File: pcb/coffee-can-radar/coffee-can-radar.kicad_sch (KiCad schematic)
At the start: 0 parts

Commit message: Add vco, attenuator and pa
First time taking kicad for a spin, it is great! Feels very familiar for
someone coming from Altium.
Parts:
- added AT?: PAT1220-C-1DB-T5, ccr-footprints:ATTN_PAT1220-C-1DB-T5, symbol ccr-library:PAT1220-C-1DB-T5
- added U?: SST11LP12, ccr-footprints:QFN-16_EP_3x3_Pitch0.5mm, symbol ccr-library:SST11LP12
- added U?: HMC431LP4E, ccr-footprints:QFN50P400X400X100-25N, symbol ccr-library:HMC431LP4E
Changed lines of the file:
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@@
 (kicad_sch (version 20211123) (generator eeschema)
   (paper "A4")
+  (symbol (lib_id "ccr-library:SST11LP12") (at 130.81 43.18 0) (unit 1)
+    (in_bom yes) (on_board yes) (fields_autoplaced)
+    (property "Reference" "U?" (id 0) (at 138.43 38.1 0))
+    (property "Value" "SST11LP12" (id 1) (at 138.43 40.64 0))
+    (property "Footprint" "ccr-footprints:QFN-16_EP_3x3_Pitch0.5mm" (id 2) (at 138.43 77.47 0)
+      (effects (font (size 1.27 1.27)) hide)
+    )
+    (property "Datasheet" "" (id 3) (at 130.81 43.18 0)
+      (effects (font (size 1.27 1.27)) hide)
+    )
+    (pin "1")
+    (pin "10")
+    (pin "11")
+    (pin "12")
+    (pin "13")
+    (pin "14")
+    (pin "15")
+    (pin "16")
+    (pin "16")
+    (pin "2")
+    (pin "3")
+    (pin "4")
+    (pin "5")
+    (pin "6")
+    (pin "7")
+    (pin "8")
+    (pin "9")
+  )
+  (symbol (lib_id "ccr-library:HMC431LP4E") (at 60.96 52.07 0) (unit 1)
+    (in_bom yes) (on_board yes) (fields_autoplaced)
+    (property "Reference" "U?" (id 0) (at 60.96 38.1 0))
+    (property "Value" "HMC431LP4E" (id 1) (at 60.96 40.64 0))
+    (property "Footprint" "ccr-footprints:QFN50P400X400X100-25N" (id 2) (at 50.8 66.04 0)
+      (effects (font (size 1.27 1.27)) (justify left bottom) hide)
+    )
+    (property "Datasheet" "" (id 3) (at 60.96 52.07 0)
+      (effects (font (size 1.27 1.27)) (justify left bottom) hide)
+    )
+    (property "MANUFACTURER" "Analog Devices" (id 4) (at 50.8 68.58 0)
+      (effects (font (size 1.27 1.27)) (justify left bottom) hide)
+    )
+    (pin "15")
+    (pin "16")
+    (pin "20")
+    (pin "22")
+    (pin "25")
+  )
+  (symbol (lib_id "ccr-library:PAT1220-C-1DB-T5") (at 106.68 50.8 0) (unit 1)
+    (in_bom yes) (on_board yes) (fields_autoplaced)
+    (property "Reference" "AT?" (id 0) (at 106.68 39.37 0))
+    (property "Value" "PAT1220-C-1DB-T5" (id 1) (at 106.68 41.91 0))
+    (property "Footprint" "ccr-footprints:ATTN_PAT1220-C-1DB-T5" (id 2) (at 109.22 60.96 0)
+      (effects (font (size 1.27 1.27)) (justify left bottom) hide)
+    )
+    (property "Datasheet" "" (id 3) (at 106.68 50.8 0)
+      (effects (font (size 1.27 1.27)) (justify left bottom) hide)
+    )
+    (property "MANUFACTURER" "SUSUMU" (id 4) (at 109.22 66.04 0)
+      (effects (font (size 1.27 1.27)) (justify left bottom) hide)
+    )
+    (property "STANDARD" "Manufacturer Recommendation" (id 5) (at 109.22 63.5 0)
+      (effects (font (size 1.27 1.27)) (justify left bottom) hide)
+    )
+    (pin "1")
+    (pin "2")
+    (pin "3")
+  )
   (sheet_instances
     (path "/" (page "1"))
   )
+  (symbol_instances
+    (path "/ecd19b5c-e315-4c28-8027-9f4a1f763db3"
+      (reference "AT?") (unit 1) (value "PAT1220-C-1DB-T5") (footprint "ccr-footprints:ATTN_PAT1220-C-1DB-T5")
+    )
+    (path "/52482f1c-9ada-4ff6-8246-b79e406c8266"
+      (reference "U?") (unit 1) (value "SST11LP12") (footprint "ccr-footprints:QFN-16_EP_3x3_Pitch0.5mm")
+    )
+    (path "/5be57fd5-b493-4486-8a3b-793a67150f96"
+      (reference "U?") (unit 1) (value "HMC431LP4E") (footprint "ccr-footprints:QFN50P400X400X100-25N")
+    )
+  )
 )

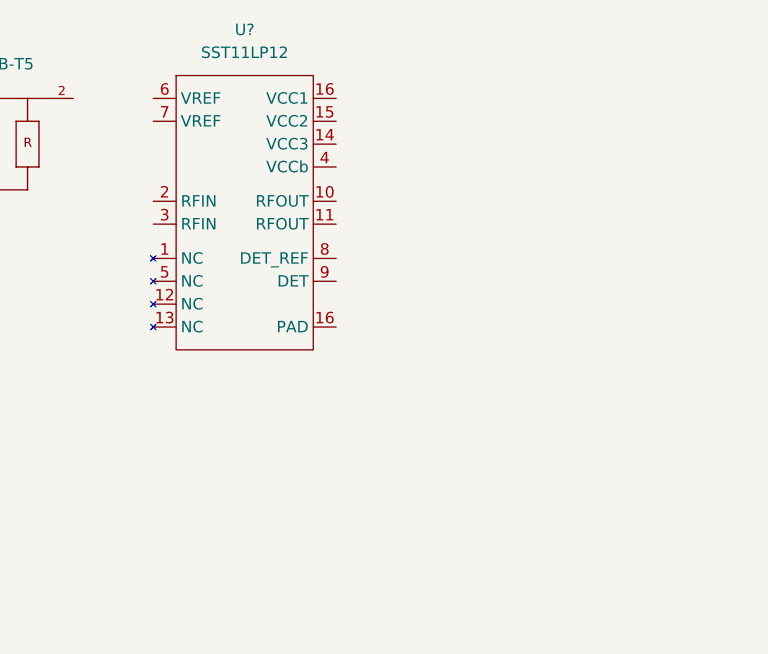
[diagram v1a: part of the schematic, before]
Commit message: Add mixer and pa
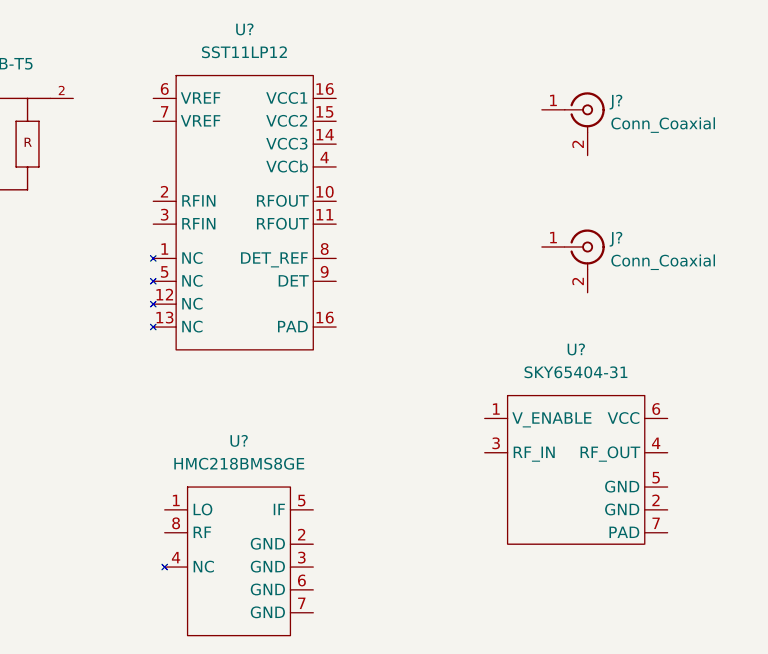
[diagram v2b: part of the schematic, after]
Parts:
- added J? (x2): Conn_Coaxial, symbol Connector:Conn_Coaxial
- added U?: SKY65404-31, ccr-footprints:SKY65404-31, symbol ccr-library:SKY65404-31
- added U?: HMC218BMS8GE, Package_SO:MSOP-8-1EP_3x3mm_P0.65mm_EP1.68x1.88mm, symbol ccr-library:HMC218BMS8GE
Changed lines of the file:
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@@
 (kicad_sch (version 20211123) (generator eeschema)
   (paper "A4")
+  (symbol (lib_id "Connector:Conn_Coaxial") (at 176.53 46.99 0) (unit 1)
+    (in_bom yes) (on_board yes) (fields_autoplaced)
+    (property "Reference" "J?" (id 0) (at 179.07 46.0131 0)
+      (effects (font (size 1.27 1.27)) (justify left))
+    )
+    (property "Value" "Conn_Coaxial" (id 1) (at 179.07 48.5531 0)
+      (effects (font (size 1.27 1.27)) (justify left))
+    )
+    (property "Footprint" "" (id 2) (at 176.53 46.99 0)
+      (effects (font (size 1.27 1.27)) hide)
+    )
+    (property "Datasheet" " ~" (id 3) (at 176.53 46.99 0)
+      (effects (font (size 1.27 1.27)) hide)
+    )
+    (pin "1")
+    (pin "2")
+  )
+  (symbol (lib_id "ccr-library:SKY65404-31") (at 167.64 78.74 0) (unit 1)
+    (in_bom yes) (on_board yes) (fields_autoplaced)
+    (property "Reference" "U?" (id 0) (at 175.26 73.66 0))
+    (property "Value" "SKY65404-31" (id 1) (at 175.26 76.2 0))
+    (property "Footprint" "ccr-footprints:SKY65404-31" (id 2) (at 181.61 99.06 0)
+      (effects (font (size 1.27 1.27)) hide)
+    )
+    (property "Datasheet" "" (id 3) (at 167.64 78.74 0)
+      (effects (font (size 1.27 1.27)) hide)
+    )
+    (pin "1")
+    (pin "2")
+    (pin "3")
+    (pin "4")
+    (pin "5")
+    (pin "6")
+    (pin "7")
+  )
   (symbol (lib_id "ccr-library:SST11LP12") (at 130.81 43.18 0) (unit 1)
     (in_bom yes) (on_board yes) (fields_autoplaced)
@@
     (pin "25")
   )
+  (symbol (lib_id "ccr-library:HMC218BMS8GE") (at 132.08 88.9 0) (unit 1)
+    (in_bom yes) (on_board yes) (fields_autoplaced)
+    (property "Reference" "U?" (id 0) (at 137.795 83.82 0))
+    (property "Value" "HMC218BMS8GE" (id 1) (at 137.795 86.36 0))
+    (property "Footprint" "Package_SO:MSOP-8-1EP_3x3mm_P0.65mm_EP1.68x1.88mm" (id 2) (at 139.7 109.22 0)
+      (effects (font (size 1.27 1.27)) hide)
+    )
+    (property "Datasheet" "" (id 3) (at 132.08 88.9 0)
+      (effects (font (size 1.27 1.27)) hide)
+    )
+    (pin "1")
+    (pin "2")
+    (pin "3")
+    (pin "4")
+    (pin "5")
+    (pin "6")
+    (pin "7")
+    (pin "8")
+  )
+  (symbol (lib_id "Connector:Conn_Coaxial") (at 176.53 62.23 0) (unit 1)
+    (in_bom yes) (on_board yes) (fields_autoplaced)
+    (property "Reference" "J?" (id 0) (at 179.07 61.2531 0)
+      (effects (font (size 1.27 1.27)) (justify left))
+    )
+    (property "Value" "Conn_Coaxial" (id 1) (at 179.07 63.7931 0)
+      (effects (font (size 1.27 1.27)) (justify left))
+    )
+    (property "Footprint" "" (id 2) (at 176.53 62.23 0)
+      (effects (font (size 1.27 1.27)) hide)
+    )
+    (property "Datasheet" " ~" (id 3) (at 176.53 62.23 0)
+      (effects (font (size 1.27 1.27)) hide)
+    )
+    (pin "1")
+    (pin "2")
+  )
   (symbol (lib_id "ccr-library:PAT1220-C-1DB-T5") (at 106.68 50.8 0) (unit 1)
     (in_bom yes) (on_board yes) (fields_autoplaced)
@@
       (reference "AT?") (unit 1) (value "PAT1220-C-1DB-T5") (footprint "ccr-footprints:ATTN_PAT1220-C-1DB-T5")
     )
+    (path "/36d17e07-64a7-424e-bc11-f3b0290e93d6"
+      (reference "J?") (unit 1) (value "Conn_Coaxial") (footprint "")
+    )
+    (path "/ea4f39a8-620c-4c83-99a6-875278db5cdb"
+      (reference "J?") (unit 1) (value "Conn_Coaxial") (footprint "")
+    )
+    (path "/40638cd4-269b-4c75-a7a3-ad362dca6ed3"
+      (reference "U?") (unit 1) (value "SKY65404-31") (footprint "ccr-footprints:SKY65404-31")
+    )
     (path "/52482f1c-9ada-4ff6-8246-b79e406c8266"
       (reference "U?") (unit 1) (value "SST11LP12") (footprint "ccr-footprints:QFN-16_EP_3x3_Pitch0.5mm")
@@
       (reference "U?") (unit 1) (value "HMC431LP4E") (footprint "ccr-footprints:QFN50P400X400X100-25N")
     )
+    (path "/77b6919d-9a80-4972-8981-2d6bb82e8279"
+      (reference "U?") (unit 1) (value "HMC218BMS8GE") (footprint "Package_SO:MSOP-8-1EP_3x3mm_P0.65mm_EP1.68x1.88mm")
+    )
   )

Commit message: Update atten
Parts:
- removed AT?: PAT1220-C-1DB-T5, ccr-footprints:ATTN_PAT1220-C-1DB-T5, symbol ccr-library:PAT1220-C-1DB-T5
- added AT?: PAT1220-C-1DB-T5, ccr-footprints:ATTN_PAT1220-C-1DB-T5, symbol ccr-library:PAT1220-C-1DB-T5
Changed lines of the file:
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@@
 (kicad_sch (version 20211123) (generator eeschema)
   (paper "A4")
+  (symbol (lib_name "PAT1220-C-1DB-T5_1") (lib_id "ccr-library:PAT1220-C-1DB-T5") (at 104.14 50.8 0) (unit 1)
+    (in_bom yes) (on_board yes) (fields_autoplaced)
+    (property "Reference" "AT?" (id 0) (at 104.14 41.91 0))
+    (property "Value" "PAT1220-C-1DB-T5" (id 1) (at 104.14 44.45 0))
+    (property "Footprint" "ccr-footprints:ATTN_PAT1220-C-1DB-T5" (id 2) (at 106.68 60.96 0)
+      (effects (font (size 1.27 1.27)) (justify left bottom) hide)
+    )
+    (property "Datasheet" "" (id 3) (at 109.22 53.34 0)
+      (effects (font (size 1.27 1.27)) (justify left bottom) hide)
+    )
+    (property "MANUFACTURER" "SUSUMU" (id 4) (at 106.68 66.04 0)
+      (effects (font (size 1.27 1.27)) (justify left bottom) hide)
+    )
+    (property "STANDARD" "Manufacturer Recommendation" (id 5) (at 106.68 63.5 0)
+      (effects (font (size 1.27 1.27)) (justify left bottom) hide)
+    )
+    (pin "1")
+    (pin "2")
+    (pin "3")
+  )
   (symbol (lib_id "Connector:Conn_Coaxial") (at 176.53 46.99 0) (unit 1)
     (in_bom yes) (on_board yes) (fields_autoplaced)
@@
     (pin "2")
   )
-  (symbol (lib_id "ccr-library:PAT1220-C-1DB-T5") (at 106.68 50.8 0) (unit 1)
-    (in_bom yes) (on_board yes) (fields_autoplaced)
-    (property "Reference" "AT?" (id 0) (at 106.68 39.37 0))
-    (property "Value" "PAT1220-C-1DB-T5" (id 1) (at 106.68 41.91 0))
-    (property "Footprint" "ccr-footprints:ATTN_PAT1220-C-1DB-T5" (id 2) (at 109.22 60.96 0)
-      (effects (font (size 1.27 1.27)) (justify left bottom) hide)
-    )
-    (property "Datasheet" "" (id 3) (at 106.68 50.8 0)
-      (effects (font (size 1.27 1.27)) (justify left bottom) hide)
-    )
-    (property "MANUFACTURER" "SUSUMU" (id 4) (at 109.22 66.04 0)
-      (effects (font (size 1.27 1.27)) (justify left bottom) hide)
-    )
-    (property "STANDARD" "Manufacturer Recommendation" (id 5) (at 109.22 63.5 0)
-      (effects (font (size 1.27 1.27)) (justify left bottom) hide)
-    )
-    (pin "1")
-    (pin "2")
-    (pin "3")
-  )
   (sheet_instances
     (path "/" (page "1"))
   )
   (symbol_instances
-    (path "/ecd19b5c-e315-4c28-8027-9f4a1f763db3"
+    (path "/0e0ec178-6f0b-4f56-acc4-f7934e7e8606"
       (reference "AT?") (unit 1) (value "PAT1220-C-1DB-T5") (footprint "ccr-footprints:ATTN_PAT1220-C-1DB-T5")
     )

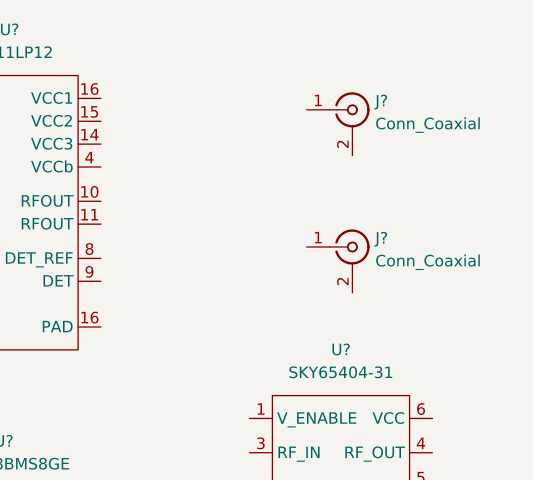
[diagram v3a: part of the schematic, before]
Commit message: Update sma connectors
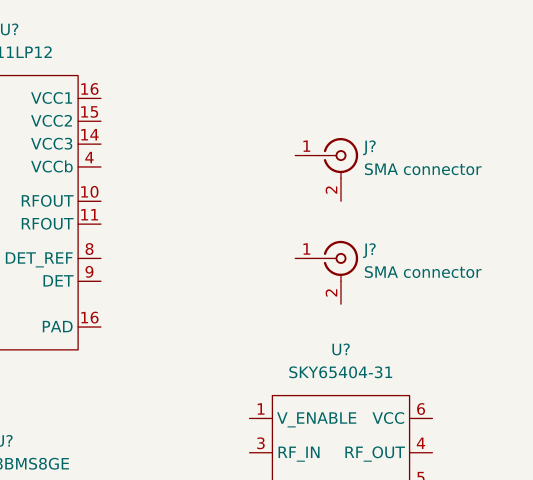
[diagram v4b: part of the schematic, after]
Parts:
- removed J? (x2): Conn_Coaxial, symbol Connector:Conn_Coaxial
- added J? (x2): SMA connector, symbol ccr-library:SMA connector
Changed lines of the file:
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@@
     (pin "3")
-  )
-  (symbol (lib_id "Connector:Conn_Coaxial") (at 176.53 46.99 0) (unit 1)
-    (in_bom yes) (on_board yes) (fields_autoplaced)
-    (property "Reference" "J?" (id 0) (at 179.07 46.0131 0)
-      (effects (font (size 1.27 1.27)) (justify left))
-    )
-    (property "Value" "Conn_Coaxial" (id 1) (at 179.07 48.5531 0)
-      (effects (font (size 1.27 1.27)) (justify left))
-    )
-    (property "Footprint" "" (id 2) (at 176.53 46.99 0)
-      (effects (font (size 1.27 1.27)) hide)
-    )
-    (property "Datasheet" " ~" (id 3) (at 176.53 46.99 0)
-      (effects (font (size 1.27 1.27)) hide)
-    )
-    (pin "1")
-    (pin "2")
   )
   (symbol (lib_id "ccr-library:SKY65404-31") (at 167.64 78.74 0) (unit 1)
@@
     (pin "25")
   )
+  (symbol (lib_id "ccr-library:SMA connector") (at 175.26 52.07 0) (unit 1)
+    (in_bom yes) (on_board yes) (fields_autoplaced)
+    (property "Reference" "J?" (id 0) (at 177.8 51.0931 0)
+      (effects (font (size 1.27 1.27)) (justify left))
+    )
+    (property "Value" "SMA connector" (id 1) (at 177.8 53.6331 0)
+      (effects (font (size 1.27 1.27)) (justify left))
+    )
+    (property "Footprint" "" (id 2) (at 175.26 52.07 0)
+      (effects (font (size 1.27 1.27)) hide)
+    )
+    (property "Datasheet" " ~" (id 3) (at 175.26 52.07 0)
+      (effects (font (size 1.27 1.27)) hide)
+    )
+    (pin "1")
+    (pin "2")
+  )
   (symbol (lib_id "ccr-library:HMC218BMS8GE") (at 132.08 88.9 0) (unit 1)
     (in_bom yes) (on_board yes) (fields_autoplaced)
@@
     (pin "8")
   )
-  (symbol (lib_id "Connector:Conn_Coaxial") (at 176.53 62.23 0) (unit 1)
+  (symbol (lib_id "ccr-library:SMA connector") (at 175.26 63.5 0) (unit 1)
     (in_bom yes) (on_board yes) (fields_autoplaced)
-    (property "Reference" "J?" (id 0) (at 179.07 61.2531 0)
+    (property "Reference" "J?" (id 0) (at 177.8 62.5231 0)
       (effects (font (size 1.27 1.27)) (justify left))
     )
-    (property "Value" "Conn_Coaxial" (id 1) (at 179.07 63.7931 0)
+    (property "Value" "SMA connector" (id 1) (at 177.8 65.0631 0)
       (effects (font (size 1.27 1.27)) (justify left))
     )
-    (property "Footprint" "" (id 2) (at 176.53 62.23 0)
+    (property "Footprint" "" (id 2) (at 175.26 63.5 0)
       (effects (font (size 1.27 1.27)) hide)
     )
-    (property "Datasheet" " ~" (id 3) (at 176.53 62.23 0)
+    (property "Datasheet" " ~" (id 3) (at 175.26 63.5 0)
       (effects (font (size 1.27 1.27)) hide)
     )
@@
       (reference "AT?") (unit 1) (value "PAT1220-C-1DB-T5") (footprint "ccr-footprints:ATTN_PAT1220-C-1DB-T5")
     )
-    (path "/36d17e07-64a7-424e-bc11-f3b0290e93d6"
-      (reference "J?") (unit 1) (value "Conn_Coaxial") (footprint "")
+    (path "/5f968713-62b6-4aff-8649-2fe586ca1b69"
+      (reference "J?") (unit 1) (value "SMA connector") (footprint "")
     )
-    (path "/ea4f39a8-620c-4c83-99a6-875278db5cdb"
-      (reference "J?") (unit 1) (value "Conn_Coaxial") (footprint "")
+    (path "/d92e5560-33f4-4fa7-a6c9-00f78704216f"
+      (reference "J?") (unit 1) (value "SMA connector") (footprint "")
     )
     (path "/40638cd4-269b-4c75-a7a3-ad362dca6ed3"

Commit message: Progress commit before going to the pub :)
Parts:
- added C? (x2): 0.5 pF, Capacitor_SMD:C_0402_1005Metric, symbol Device:C
- added C?: 0.1 uF, Capacitor_SMD:C_0402_1005Metric, symbol Device:C
- added C? (x3): 100nF, Capacitor_SMD:C_0402_1005Metric, symbol Device:C
- added C?: 1.8pF, Capacitor_SMD:C_0402_1005Metric, symbol Device:C
- added C?: 4.7 uF 6.3V, Capacitor_SMD:C_0603_1608Metric, symbol Device:C
- added C? (x2): 10 pF, Capacitor_SMD:C_0402_1005Metric, symbol Device:C
- added C?: 10 nF, Capacitor_SMD:C_0402_1005Metric, symbol Device:C
- added C?: 2.2uF, Capacitor_SMD:C_0603_1608Metric, symbol Device:C
- added L?: 0.6 nH, symbol Device:L
- added R?: 100, Resistor_SMD:R_0402_1005Metric, symbol Device:R_Small_US
- added U?: MCP1700-3002E_SOT23, Package_TO_SOT_SMD:SOT-23, symbol Regulator_Linear:MCP1700-3002E_SOT23
- added U?: WILKINSON_DIVIDER, symbol ccr-library:WILKINSON_DIVIDER
- AT?: value PAT1220-C-1DB-T5 -> PAT1220-C-7DB-T5
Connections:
- net at AT?.1: now also U?.16 (RFOUT)
- net GND: now reaches AT?.3
- net GND: now also U?.15 (GND), U?.16 (VCC1), U?.2 (GND), U?.25 (EXP), U?.5 (GND), U?.7 (PAD), C?.2, C?.2, C?.2, C?.2, C?.2, C?.2, C?.2, C?.2, C?.2, C?.2, C?.2, C?.2, U?.1 (GND)
- net at U?.1 (V_ENABLE): now also R?.1
- net at U?.3 (RF_IN): now also J?.1 (In), C?.1
- net at U?.6 (VCC): now also L?.2
- net at U?.10 (RFOUT): now also U?.11 (RFOUT), C?.1
- net +3V3: now reaches U?.14 (VCC3)
- net +3V3: now also U?.15 (VCC2), U?.16 (VCC1), U?.4 (VCCb), C?.1, C?.1, C?.1, C?.1, C?.1, U?.3 (VI)
- net at U?.8 (DET_REF): now also C?.1
- net at U?.9 (DET): now also C?.1
- net +3V0: now reaches U?.20 (VCC)
- net +3V0: now also C?.1, C?.1, C?.1, L?.1, R?.2, U?.2 (VO)
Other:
- moved on the sheet: AT?, J?, U?
